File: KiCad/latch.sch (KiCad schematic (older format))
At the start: 14 parts

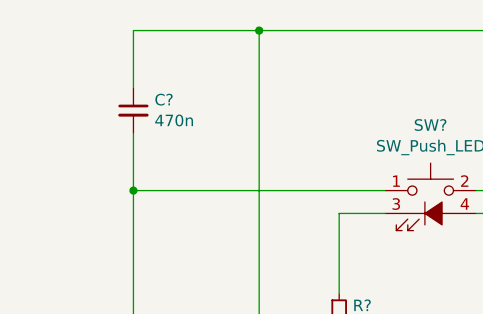
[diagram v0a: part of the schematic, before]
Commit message: changed 4053 to DG419 & added negative latch
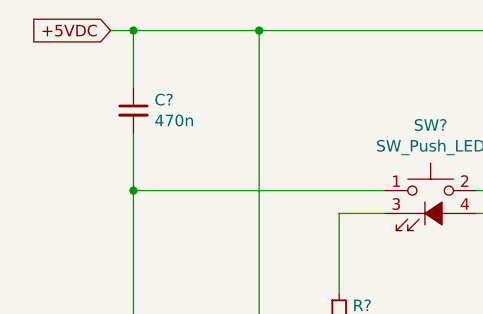
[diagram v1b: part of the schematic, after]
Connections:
- net +5VDC: now reaches C?.1, Q?.3 (E), Q?.3 (E), R?.1
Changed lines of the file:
@@
 $Descr A4 11693 8268
 encoding utf-8
-Sheet 6 6
+Sheet 5 8
 Title ""
 Date ""
@@
 AR Path="/605C72FC/605C8BFA" Ref="Q?"  Part="1"
 AR Path="/605ED2C3/605C8BFA" Ref="Q?"  Part="1"
+AR Path="/606576F1/605C8BFA" Ref="Q?"  Part="1"
 F 0 "Q?" H 6691 4896 50  0000 L CNN
 F 1 "Q_NPN_BCE" H 6691 4805 50  0000 L CNN
@@
 AR Path="/605C72FC/605CA6A1" Ref="R?"  Part="1"
 AR Path="/605ED2C3/605CA6A1" Ref="R?"  Part="1"
+AR Path="/606576F1/605CA6A1" Ref="R?"  Part="1"
 F 0 "R?" H 4409 4246 50  0000 L CNN
 F 1 "10k" H 4409 4155 50  0000 L CNN
@@
 AR Path="/605C72FC/605D57B8" Ref="C?"  Part="1"
 AR Path="/605ED2C3/605D57B8" Ref="C?"  Part="1"
+AR Path="/606576F1/605D57B8" Ref="C?"  Part="1"
 F 0 "C?" H 4442 3246 50  0000 L CNN
 F 1 "470n" H 4442 3155 50  0000 L CNN
@@
 AR Path="/605C72FC/605D5FB7" Ref="SW?"  Part="1"
 AR Path="/605ED2C3/605D5FB7" Ref="SW?"  Part="1"
+AR Path="/606576F1/605D5FB7" Ref="SW?"  Part="1"
 F 0 "SW?" H 5650 4035 50  0000 C CNN
 F 1 "SW_Push_LED" H 5650 3944 50  0000 C CNN
@@
 AR Path="/605C72FC/605D75B4" Ref="Q?"  Part="1"
 AR Path="/605ED2C3/605D75B4" Ref="Q?"  Part="1"
+AR Path="/606576F1/605D75B4" Ref="Q?"  Part="1"
 F 0 "Q?" H 5191 4404 50  0000 L CNN
 F 1 "Q_PNP_BCE" H 5191 4495 50  0000 L CNN
@@
 AR Path="/605C72FC/605D8BBC" Ref="R?"  Part="1"
 AR Path="/605ED2C3/605D8BBC" Ref="R?"  Part="1"
+AR Path="/606576F1/605D8BBC" Ref="R?"  Part="1"
 F 0 "R?" H 4409 5246 50  0000 L CNN
 F 1 "10k" H 4409 5155 50  0000 L CNN
@@
 AR Path="/605C72FC/605D9138" Ref="#PWR?"  Part="1"
 AR Path="/605ED2C3/605D9138" Ref="#PWR?"  Part="1"
+AR Path="/606576F1/605D9138" Ref="#PWR?"  Part="1"
 F 0 "#PWR?" H 4350 5250 50  0001 C CNN
 F 1 "GND" H 4355 5327 50  0000 C CNN
@@
 AR Path="/605C72FC/605D988B" Ref="R?"  Part="1"
 AR Path="/605ED2C3/605D988B" Ref="R?"  Part="1"
+AR Path="/606576F1/605D988B" Ref="R?"  Part="1"
 F 0 "R?" V 5854 4450 50  0000 C CNN
 F 1 "10k" V 5945 4450 50  0000 C CNN
@@
 AR Path="/605C72FC/605DA2A0" Ref="R?"  Part="1"
 AR Path="/605ED2C3/605DA2A0" Ref="R?"  Part="1"
+AR Path="/606576F1/605DA2A0" Ref="R?"  Part="1"
 F 0 "R?" H 6341 3996 50  0000 R CNN
 F 1 "10k" H 6341 3905 50  0000 R CNN
@@
 AR Path="/605C72FC/605DAF7B" Ref="R?"  Part="1"
 AR Path="/605ED2C3/605DAF7B" Ref="R?"  Part="1"
+AR Path="/606576F1/605DAF7B" Ref="R?"  Part="1"
 F 0 "R?" H 6459 3246 50  0000 L CNN
 F 1 "470k" H 6459 3155 50  0000 L CNN
@@
 AR Path="/605C72FC/605DB9E1" Ref="R?"  Part="1"
 AR Path="/605ED2C3/605DB9E1" Ref="R?"  Part="1"
+AR Path="/606576F1/605DB9E1" Ref="R?"  Part="1"
 F 0 "R?" V 6654 3550 50  0000 C CNN
 F 1 "10k" V 6745 3550 50  0000 C CNN
@@
 AR Path="/605C72FC/605DC332" Ref="Q?"  Part="1"
 AR Path="/605ED2C3/605DC332" Ref="Q?"  Part="1"
+AR Path="/606576F1/605DC332" Ref="Q?"  Part="1"
 F 0 "Q?" H 7590 3504 50  0000 L CNN
 F 1 "Q_PNP_BCE" H 7590 3595 50  0000 L CNN
@@
 AR Path="/605C72FC/605DDA9F" Ref="R?"  Part="1"
 AR Path="/605ED2C3/605DDA9F" Ref="R?"  Part="1"
+AR Path="/606576F1/605DDA9F" Ref="R?"  Part="1"
 F 0 "R?" H 7441 4146 50  0000 R CNN
 F 1 "100k" H 7441 4055 50  0000 R CNN
@@
 AR Path="/605C72FC/605DF842" Ref="R?"  Part="1"
 AR Path="/605ED2C3/605DF842" Ref="R?"  Part="1"
+AR Path="/606576F1/605DF842" Ref="R?"  Part="1"
 F 0 "R?" H 7441 5196 50  0000 R CNN
 F 1 "1M" H 7441 5105 50  0000 R CNN
@@
 AR Path="/605C72FC/605E2C4C" Ref="R?"  Part="1"
 AR Path="/605ED2C3/605E2C4C" Ref="R?"  Part="1"
+AR Path="/606576F1/605E2C4C" Ref="R?"  Part="1"
 F 0 "R?" H 5309 4146 50  0000 L CNN
 F 1 "220" H 5309 4055 50  0000 L CNN
@@
 Wire Wire Line
 	7650 4500 7500 4500
+Wire Wire Line
+	4250 2850 4350 2850
+Connection ~ 4350 2850
+Text GLabel 4250 2850 0    50   Input ~ 0
++5VDC
 $EndSCHEMATC
